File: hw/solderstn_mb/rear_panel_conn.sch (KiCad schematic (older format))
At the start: 16 parts, among them J1201 Conn_02x05_Odd_Even, J1202 USB_B-TE_1734346-1, J1203 DB9_Male_MountingHoles, J1204 USB_A-TE_1-292303-1, U1201 USBLC6-2SC6, U1202 74LVC2G17, U1203 USBLC6-2SC6, U601 74LVC2G17

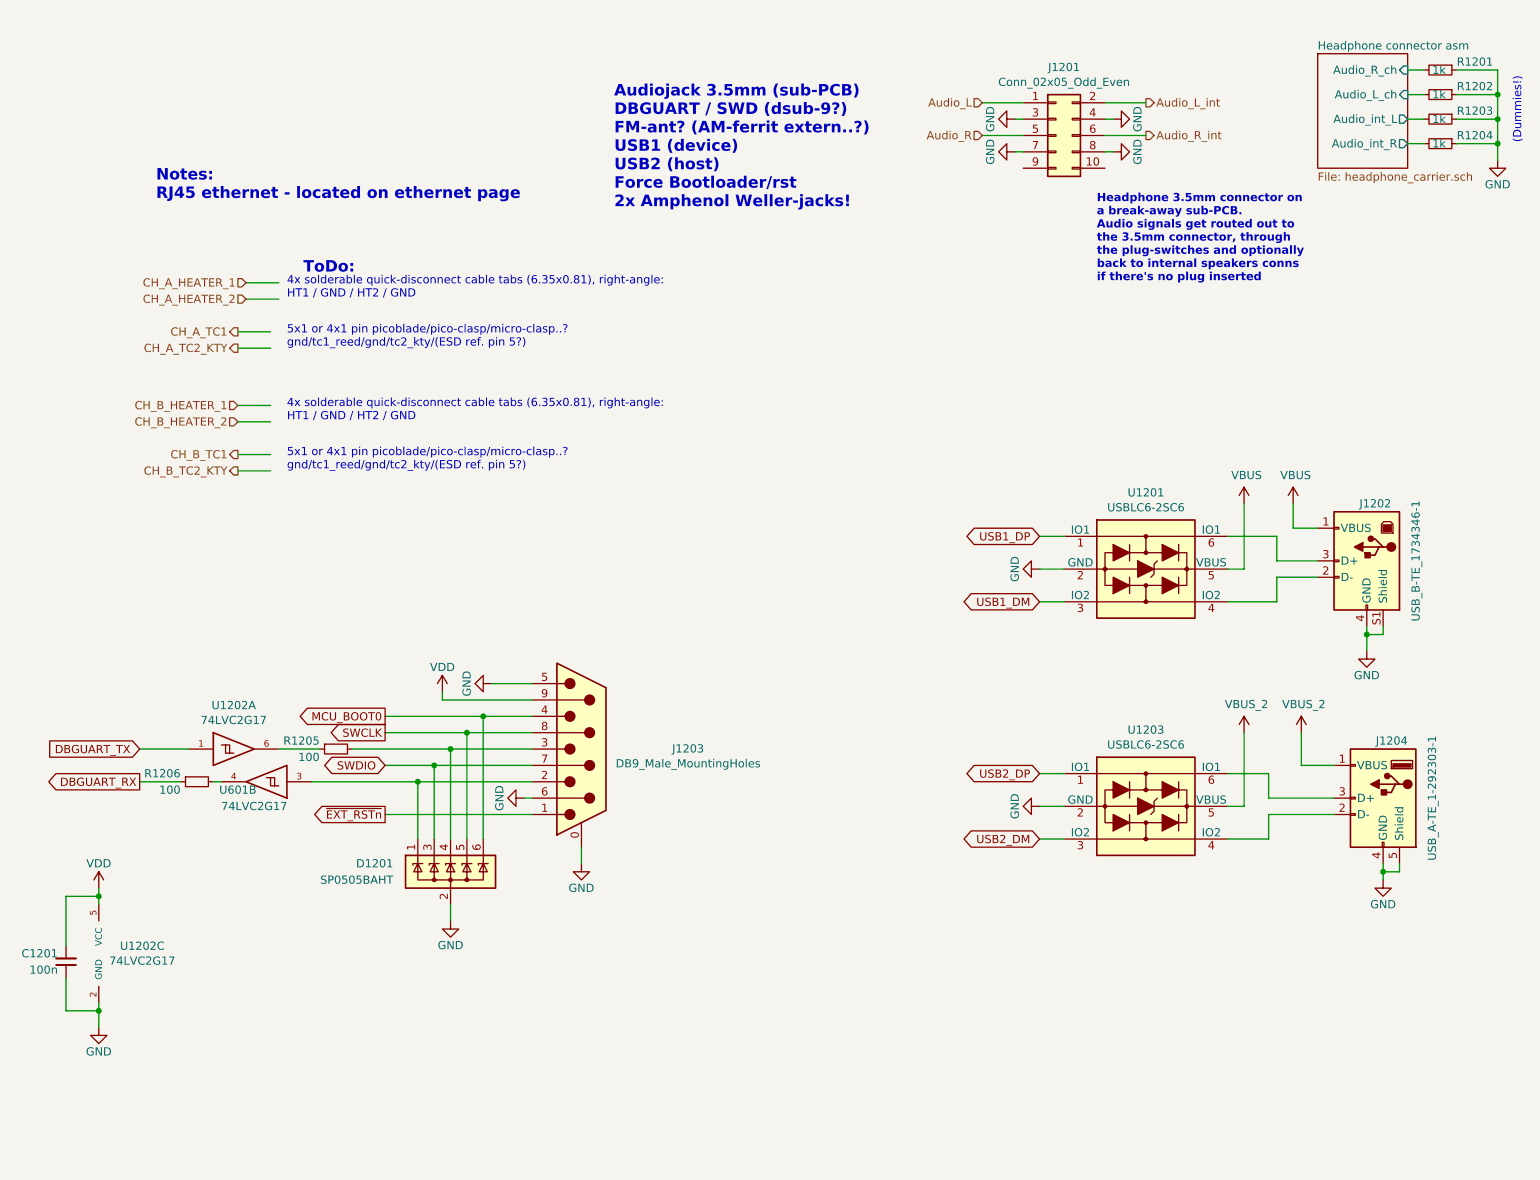
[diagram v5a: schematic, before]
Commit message: Corrected several ERC issues. Re-annotated & assigned all footprints except 32k xtal (will prob. replace with RTC module anyway)
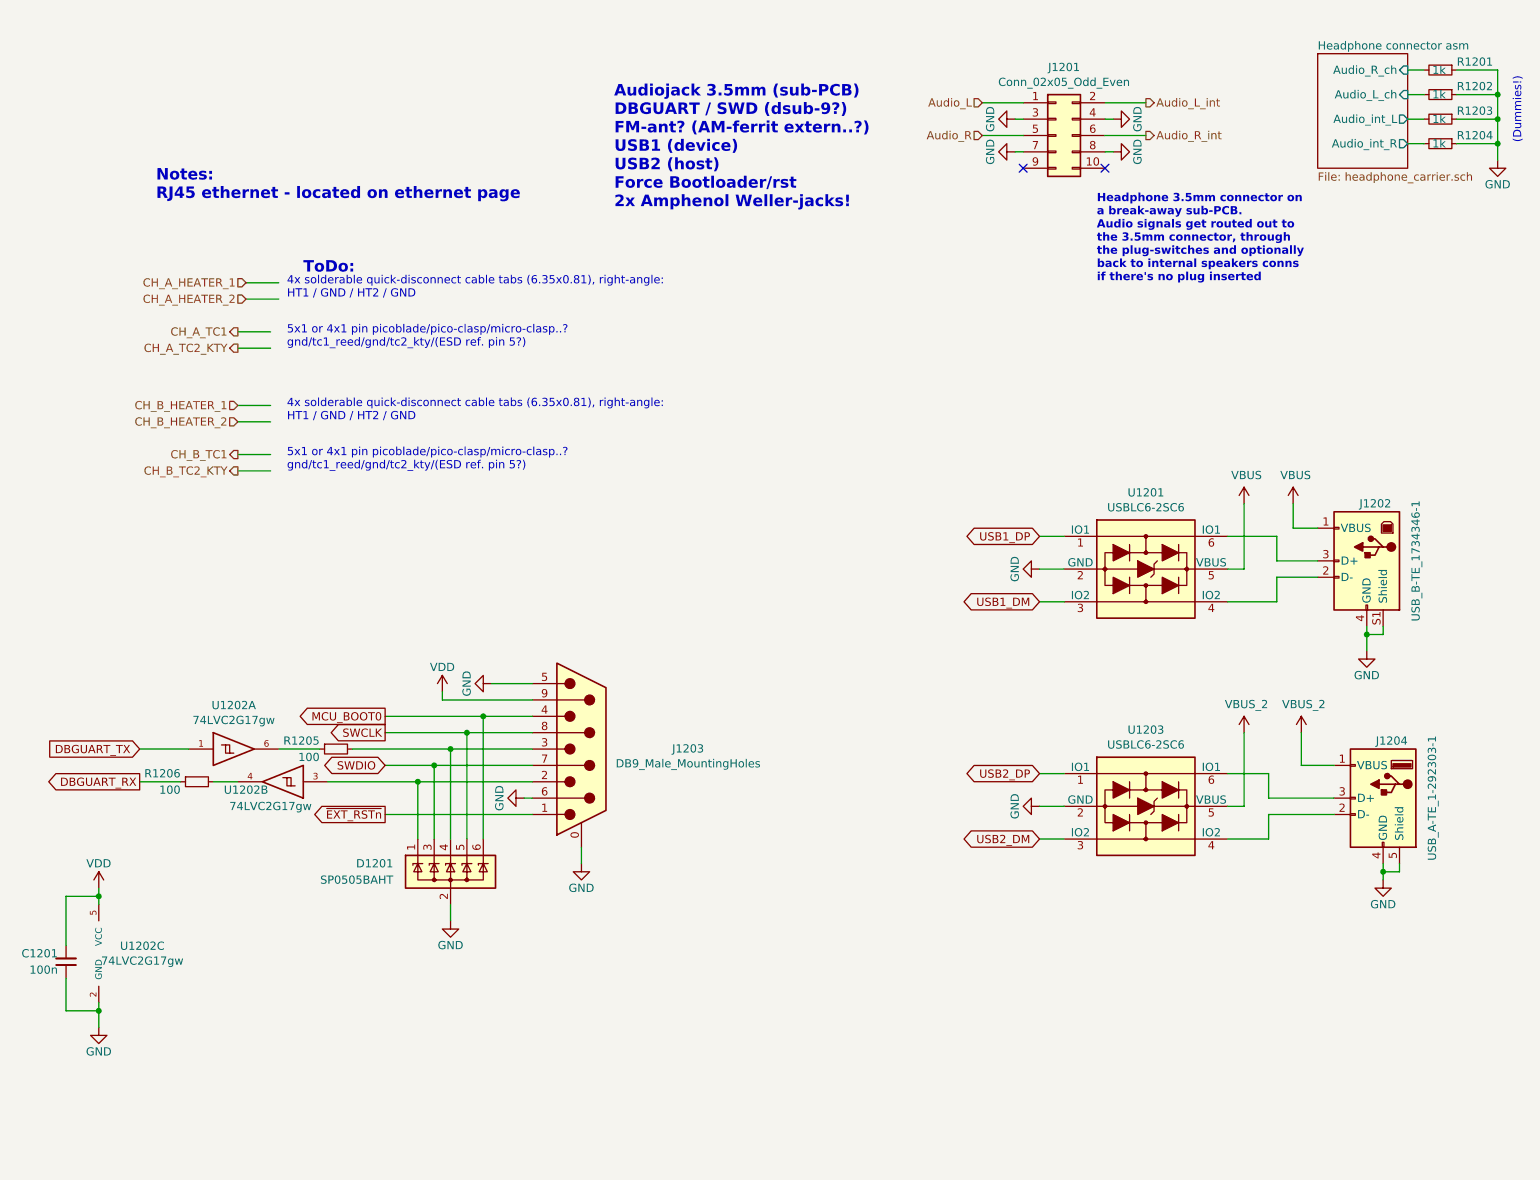
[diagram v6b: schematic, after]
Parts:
- C1201: footprint (none) -> Capacitor_SMD:C_0603_1608Metric
- R1201, R1202, R1203, R1204: footprint (none) -> Resistor_SMD:R_0402_1005Metric
- R1205, R1206: footprint (none) -> Resistor_SMD:R_0603_1608Metric
- U1201, U1203: footprint TO_SOT_Packages_SMD:SOT-23-6 -> Package_TO_SOT_SMD:SOT-23-6_Handsoldering
- U1202: value 74LVC2G17 -> 74LVC2G17gw; footprint (none) -> Package_TO_SOT_SMD:SOT-363_SC-70-6_Handsoldering
- U1202: renamed from U601; value 74LVC2G17 -> 74LVC2G17gw; footprint (none) -> Package_TO_SOT_SMD:SOT-363_SC-70-6_Handsoldering
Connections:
- no-connect marks 0 -> 2
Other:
- moved on the sheet: U1202B
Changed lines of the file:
@@
 F 0 "U1203" H 7800 6017 50  0000 C CNN
 F 1 "USBLC6-2SC6" H 7800 5926 50  0000 C CNN
-F 2 "TO_SOT_Packages_SMD:SOT-23-6" H 8450 5900 50  0001 C CNN
+F 2 "Package_TO_SOT_SMD:SOT-23-6_Handsoldering" H 8450 5900 50  0001 C CNN
 F 3 "" H 7550 5900 50  0001 C CNN
 	1    7800 5550
@@
 F 0 "U1201" H 7800 4567 50  0000 C CNN
 F 1 "USBLC6-2SC6" H 7800 4476 50  0000 C CNN
-F 2 "TO_SOT_Packages_SMD:SOT-23-6" H 8450 4450 50  0001 C CNN
+F 2 "Package_TO_SOT_SMD:SOT-23-6_Handsoldering" H 8450 4450 50  0001 C CNN
 F 3 "" H 7550 4450 50  0001 C CNN
 	1    7800 4100
@@
 F 0 "R1201" V 9550 1150 50  0000 L CNN
 F 1 "1k" V 9600 1000 50  0000 L CNN
-F 2 "" H 9600 1050 50  0001 C CNN
+F 2 "Resistor_SMD:R_0402_1005Metric" H 9600 1050 50  0001 C CNN
 F 3 "~" H 9600 1050 50  0001 C CNN
 	1    9600 1050
@@
 F 0 "R1202" V 9550 1300 50  0000 L CNN
 F 1 "1k" V 9600 1150 50  0000 L CNN
-F 2 "" H 9600 1200 50  0001 C CNN
+F 2 "Resistor_SMD:R_0402_1005Metric" H 9600 1200 50  0001 C CNN
 F 3 "~" H 9600 1200 50  0001 C CNN
 	1    9600 1200
@@
 F 0 "R1203" V 9550 1450 50  0000 L CNN
 F 1 "1k" V 9600 1300 50  0000 L CNN
-F 2 "" H 9600 1350 50  0001 C CNN
+F 2 "Resistor_SMD:R_0402_1005Metric" H 9600 1350 50  0001 C CNN
 F 3 "~" H 9600 1350 50  0001 C CNN
 	1    9600 1350
@@
 F 0 "R1204" V 9550 1600 50  0000 L CNN
 F 1 "1k" V 9600 1450 50  0000 L CNN
-F 2 "" H 9600 1500 50  0001 C CNN
+F 2 "Resistor_SMD:R_0402_1005Metric" H 9600 1500 50  0001 C CNN
 F 3 "~" H 9600 1500 50  0001 C CNN
 	1    9600 1500
@@
 P 2250 5200
 F 0 "U1202" H 2225 5467 50  0000 C CNN
-F 1 "74LVC2G17" H 2225 5376 50  0000 C CNN
-F 2 "" H 2250 5200 50  0001 C CNN
+F 1 "74LVC2G17gw" H 2225 5376 50  0000 C CNN
+F 2 "Package_TO_SOT_SMD:SOT-363_SC-70-6_Handsoldering" H 2250 5200 50  0001 C CNN
 F 3 "http://www.ti.com/lit/sg/scyt129e/scyt129e.pdf" H 2250 5200 50  0001 C CNN
 	1    2250 5200
@@
 $EndComp
 $Comp
-L customlib_mj:74LVC2G17 U601
+L customlib_mj:74LVC2G17 U1202
 U 2 1 5F9A89B3
-P 2400 5400
-F 0 "U601" H 2550 5450 50  0000 C CNN
-F 1 "74LVC2G17" H 2450 5550 50  0000 C CNN
-F 2 "" H 2400 5400 50  0001 C CNN
-F 3 "http://www.ti.com/lit/sg/scyt129e/scyt129e.pdf" H 2400 5400 50  0001 C CNN
-	2    2400 5400
+P 2500 5400
+F 0 "U1202" H 2700 5450 50  0000 C CNN
+F 1 "74LVC2G17gw" H 2550 5550 50  0000 C CNN
+F 2 "Package_TO_SOT_SMD:SOT-363_SC-70-6_Handsoldering" H 2500 5400 50  0001 C CNN
+F 3 "http://www.ti.com/lit/sg/scyt129e/scyt129e.pdf" H 2500 5400 50  0001 C CNN
+	2    2500 5400
 	-1   0    0    1
 $EndComp
@@
 P 1400 6450
 F 0 "U1202" H 1666 6496 50  0000 C CNN
-F 1 "74LVC2G17" H 1666 6405 50  0000 C CNN
-F 2 "" H 1400 6450 50  0001 C CNN
+F 1 "74LVC2G17gw" H 1666 6405 50  0000 C CNN
+F 2 "Package_TO_SOT_SMD:SOT-363_SC-70-6_Handsoldering" H 1400 6450 50  0001 C CNN
 F 3 "http://www.ti.com/lit/sg/scyt129e/scyt129e.pdf" H 1400 6450 50  0001 C CNN
 	3    1400 6450
@@
 F 0 "R1205" V 2800 5300 50  0000 L CNN
 F 1 "100" V 2900 5300 50  0000 L CNN
-F 2 "" H 2850 5200 50  0001 C CNN
+F 2 "Resistor_SMD:R_0603_1608Metric" H 2850 5200 50  0001 C CNN
 F 3 "~" H 2850 5200 50  0001 C CNN
 	1    2850 5200
@@
 F 0 "R1206" V 1950 5500 50  0000 L CNN
 F 1 "100" V 2050 5500 50  0000 L CNN
-F 2 "" H 2000 5400 50  0001 C CNN
+F 2 "Resistor_SMD:R_0603_1608Metric" H 2000 5400 50  0001 C CNN
 F 3 "~" H 2000 5400 50  0001 C CNN
 	1    2000 5400
@@
 $EndComp
 Wire Wire Line
-	2150 5400 2100 5400
+	2250 5400 2100 5400
 Wire Wire Line
 	1900 5400 1650 5400
@@
 F 0 "C1201" H 1250 6450 50  0000 L CNN
 F 1 "100n" H 1250 6550 50  0000 L CNN
-F 2 "" H 1200 6500 50  0001 C CNN
+F 2 "Capacitor_SMD:C_0603_1608Metric" H 1200 6500 50  0001 C CNN
 F 3 "~" H 1200 6500 50  0001 C CNN
 	1    1200 6500
@@
 Connection ~ 3350 5400
 Wire Wire Line
-	3350 5400 2700 5400
+	3350 5400 2800 5400
 Wire Wire Line
 	3450 5750 3450 5300
@@
 Text Notes 2650 2300 0    70   ~ 14
 ToDo:
+NoConn ~ 7050 1650
+NoConn ~ 7550 1650
 $EndSCHEMATC

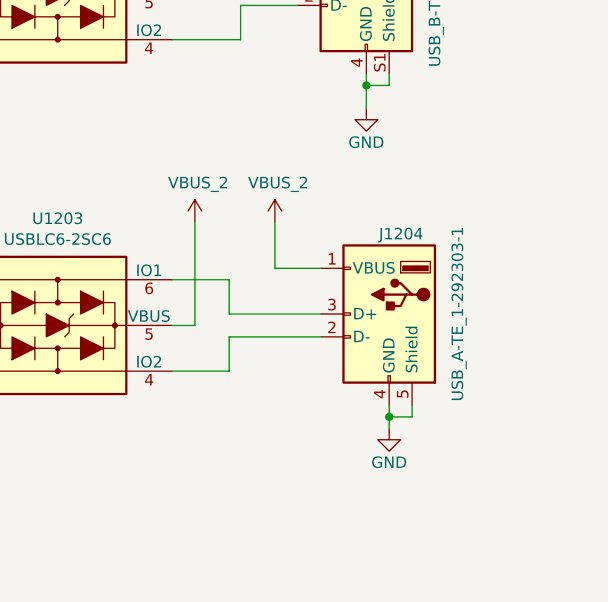
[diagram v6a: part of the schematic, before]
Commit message: Updated USB-A conn to CUI UJ2-AH-1-SMT because retention pads are SMD. Also better USB-A cutout in back panel. Updated 3d test model
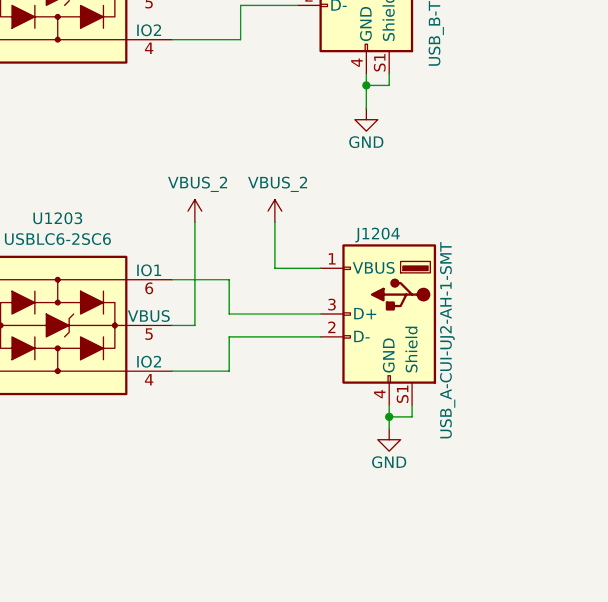
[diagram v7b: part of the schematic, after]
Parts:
- removed J1204: USB_A-TE_1-292303-1, customlib_mj_fp:TE_1-292303-1, symbol customlib_mj:USB_A-TE_1-292303-1
- added J1204: USB_A-CUI-UJ2-AH-1-SMT, customlib_mj_fp:CUI-UJ2_AH_1_SMT, symbol customlib_mj:USB_A-CUI-UJ2-AH-1-SMT
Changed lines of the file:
@@
 Notes:\nRJ45 ethernet - located on ethernet page\n
-$Comp
-L customlib_mj:USB_A-TE_1-292303-1 J1204
-U 1 1 5F769C5C
-P 9250 5500
-F 0 "J1204" H 9100 5850 50  0000 L CNN
-F 1 "USB_A-TE_1-292303-1" V 8950 5500 50  0000 C CNN
-F 2 "customlib_mj_fp:TE_1-292303-1" H 9400 5450 50  0001 C CNN
-F 3 "https://www.te.com/usa-en/product-1-292303-1.html" H 9400 5450 50  0001 C CNN
-	1    9250 5500
-	-1   0    0    -1
-$EndComp
 $Comp
 L customlib_mj:USB_B-TE_1734346-1 J1202
@@
 NoConn ~ 7050 1650
 NoConn ~ 7550 1650
+$Comp
+L customlib_mj:USB_A-CUI-UJ2-AH-1-SMT J1204
+U 1 1 5F7D7CD9
+P 9250 5500
+F 0 "J1204" H 9200 5850 50  0000 L CNN
+F 1 "USB_A-CUI-UJ2-AH-1-SMT" V 9000 4950 50  0000 L CNN
+F 2 "customlib_mj_fp:CUI-UJ2_AH_1_SMT" H 9400 5450 50  0001 C CNN
+F 3 "https://www.cuidevices.com/product/interconnect/connectors/usb-connectors/uj2-ah-smt-series/uj2-ah-1-smt" H 9400 5450 50  0001 C CNN
+	1    9250 5500
+	-1   0    0    -1
+$EndComp
 $EndSCHEMATC
